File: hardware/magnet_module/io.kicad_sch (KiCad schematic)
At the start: 17 parts, among them J10 Conn_Coaxial, J11 Conn_Coaxial, J12 Conn_Coaxial, J13 Conn_Coaxial, J14 Conn_Coaxial, J15 Conn_Coaxial, J16 Conn_01x04_Pin, J17 Conn_01x04_Pin, J18 Conn_01x03_Pin, J19 Conn_01x03_Pin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

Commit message: add titles & esd protection for IO
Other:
- company: (none) -> Christie Lab, CU-Anschultz
- title: (none) -> Autotrainer Magnet Module - External IO
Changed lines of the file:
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@@
 	(generator_version "8.0")
 	(paper "A4")
+	(title_block
+		(title "Autotrainer Magnet Module - External IO")
+		(date "2024-07-09")
+		(rev "v1.0")
+		(company "Christie Lab, CU-Anschultz")
+		(comment 1 "Prepared by LeafLabs, LLC")
+	)
 	(junction
 		(at 45.72 35.56)

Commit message: add all PNs, relevant datasheets, and test points
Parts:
- C20, C21, C22, C23: footprint (none) -> Capacitor_SMD:C_0603_1608Metric; MPN (none) -> CC0603KRX7R7BB104
- J10, J11, J12, J13, J14, J15: MPN (none) -> CONMHF1-SMD-T
- J16, J17: MPN (none) -> BM04B-SRSS-TB
- J18, J19: MPN (none) -> BM03B-SRSS-TB
- R12, R13: MPN (none) -> RC0603FR-0710KL
- U10: MPN (none) -> TXB0104RUT
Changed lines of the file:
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@@
 			)
 		)
-		(property "Footprint" ""
+		(property "Footprint" "Capacitor_SMD:C_0603_1608Metric"
 			(at 46.0248 71.12 0)
 			(effects
@@
 			)
 		)
-		(property "MPN" ""
+		(property "MPN" "CC0603KRX7R7BB104"
 			(at 46.99 67.31 0)
 			(effects
@@
 			)
 		)
+		(property "MPN" "BM03B-SRSS-TB"
+			(at 260.35 82.55 0)
+			(effects
+				(font
+					(size 1.27 1.27)
+				)
+				(hide yes)
+			)
+		)
 		(pin "2"
 		)
@@
 			)
 		)
+		(property "MPN" "BM04B-SRSS-TB"
+			(at 260.35 50.8 0)
+			(effects
+				(font
+					(size 1.27 1.27)
+				)
+				(hide yes)
+			)
+		)
 		(pin "1"
 		)
@@
 			)
 		)
-		(property "MPN" ""
+		(property "MPN" "RC0603FR-0710KL"
 			(at 41.91 31.75 0)
 			(effects
@@
 			)
 		)
+		(property "MPN" "CONMHF1-SMD-T"
+			(at 54.61 35.56 0)
+			(effects
+				(font
+					(size 1.27 1.27)
+				)
+				(hide yes)
+			)
+		)
 		(pin "1"
 		)
@@
 			)
 		)
+		(property "MPN" "CONMHF1-SMD-T"
+			(at 100.33 120.65 0)
+			(effects
+				(font
+					(size 1.27 1.27)
+				)
+				(hide yes)
+			)
+		)
 		(pin "1"
 		)
@@
 			)
 		)
-		(property "Footprint" ""
+		(property "Footprint" "Capacitor_SMD:C_0603_1608Metric"
 			(at 62.23 108.2548 0)
 			(effects
@@
 			)
 		)
-		(property "MPN" ""
+		(property "MPN" "CC0603KRX7R7BB104"
 			(at 58.42 109.22 0)
 			(effects
@@
 		)
 		(property "Description" "coaxial connector (BNC, SMA, SMB, SMC, Cinch/RCA, LEMO, ...)"
+			(at 100.33 135.89 0)
+			(effects
+				(font
+					(size 1.27 1.27)
+				)
+				(hide yes)
+			)
+		)
+		(property "MPN" "CONMHF1-SMD-T"
 			(at 100.33 135.89 0)
 			(effects
@@
 			)
 		)
-		(property "MPN" ""
+		(property "MPN" "RC0603FR-0710KL"
 			(at 43.18 59.69 0)
 			(effects
@@
 			)
 		)
+		(property "MPN" "CONMHF1-SMD-T"
+			(at 100.33 154.94 0)
+			(effects
+				(font
+					(size 1.27 1.27)
+				)
+				(hide yes)
+			)
+		)
 		(pin "1"
 		)
@@
 		)
 		(property "Description" "4-Bit Bidirectional Voltage-Level Translator, Auto Direction Sensing and ±15-kV ESD Protection, 1.2 - 3.6V APort, 1.65 - 5.5V BPort, Texas_PUQFN-12"
+			(at 52.07 129.54 0)
+			(effects
+				(font
+					(size 1.27 1.27)
+				)
+				(hide yes)
+			)
+		)
+		(property "MPN" "TXB0104RUT"
 			(at 52.07 129.54 0)
 			(effects
@@
 			)
 		)
-		(property "Footprint" ""
+		(property "Footprint" "Capacitor_SMD:C_0603_1608Metric"
 			(at 41.91 108.2548 0)
 			(effects
@@
 			)
 		)
-		(property "MPN" ""
+		(property "MPN" "CC0603KRX7R7BB104"
 			(at 45.72 109.22 0)
 			(effects
@@
 			)
 		)
-		(property "Footprint" ""
+		(property "Footprint" "Capacitor_SMD:C_0603_1608Metric"
 			(at 44.7548 43.18 0)
 			(effects
@@
 			)
 		)
-		(property "MPN" ""
+		(property "MPN" "CC0603KRX7R7BB104"
 			(at 45.72 39.37 0)
 			(effects
@@
 			)
 		)
+		(property "MPN" "BM04B-SRSS-TB"
+			(at 260.35 36.83 0)
+			(effects
+				(font
+					(size 1.27 1.27)
+				)
+				(hide yes)
+			)
+		)
 		(pin "1"
 		)
@@
 			)
 		)
+		(property "MPN" "CONMHF1-SMD-T"
+			(at 55.88 63.5 0)
+			(effects
+				(font
+					(size 1.27 1.27)
+				)
+				(hide yes)
+			)
+		)
 		(pin "1"
 		)
@@
 		)
 		(property "Description" "coaxial connector (BNC, SMA, SMB, SMC, Cinch/RCA, LEMO, ...)"
+			(at 100.33 104.14 0)
+			(effects
+				(font
+					(size 1.27 1.27)
+				)
+				(hide yes)
+			)
+		)
+		(property "MPN" "CONMHF1-SMD-T"
 			(at 100.33 104.14 0)
 			(effects
@@
 			(at 260.35 69.85 0)
 			(effects
+				(font
+					(size 1.27 1.27)
+				)
+				(hide yes)
+			)
+		)
+		(property "MPN" "BM03B-SRSS-TB"
+			(at 260.35 69.85 0)
+			(effects

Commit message: make changes as requested by Ryan
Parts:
- removed C22, C23: 0.1uF, Capacitor_SMD:C_0603_1608Metric, symbol Device:C
- removed J12, J13, J14, J15: Conn_Coaxial, symbol Connector:Conn_Coaxial
- removed U10: TXB0104RUT, Package_DFN_QFN:Texas_R-PUQFN-N12, symbol Logic_LevelTranslator:TXB0104RUT
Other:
- note removed: "External Equipment"
- company: Christie Lab, CU-Anschultz -> Christie Lab, CU-Anschutz

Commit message: make changes requested by dan, run ERC
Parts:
- removed J18, J19: Conn_01x03_Pin, symbol Connector:Conn_01x03_Pin
- added J13, J14: Conn_01x02_Pin, symbol Connector:Conn_01x02_Pin
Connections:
- net GND: now also J13.1 (Pin_1), J14.1 (Pin_1)
- net GPIO0: now also J13.2 (Pin_2)
- net GPIO1: now also J14.2 (Pin_2)
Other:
- note added: "Teensy Connection"

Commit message: update PNs for BNC connectors and motor connectors
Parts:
- J10, J11: MPN CONMHF1-SMD-T -> CONBNC002
- J16, J17: MPN BM04B-SRSS-TB -> SM04B-SRSS-TB
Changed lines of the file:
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@@
 			)
 		)
-		(property "MPN" "BM04B-SRSS-TB"
+		(property "MPN" "SM04B-SRSS-TB"
 			(at 260.35 50.8 0)
 			(effects
@@
 			)
 		)
-		(property "MPN" "CONMHF1-SMD-T"
+		(property "MPN" "CONBNC002"
 			(at 54.61 35.56 0)
 			(effects
@@
 			)
 		)
-		(property "MPN" "BM04B-SRSS-TB"
+		(property "MPN" "SM04B-SRSS-TB"
 			(at 260.35 36.83 0)
 			(effects
@@
 			)
 		)
-		(property "MPN" "CONMHF1-SMD-T"
+		(property "MPN" "CONBNC002"
 			(at 55.88 63.5 0)
 			(effects

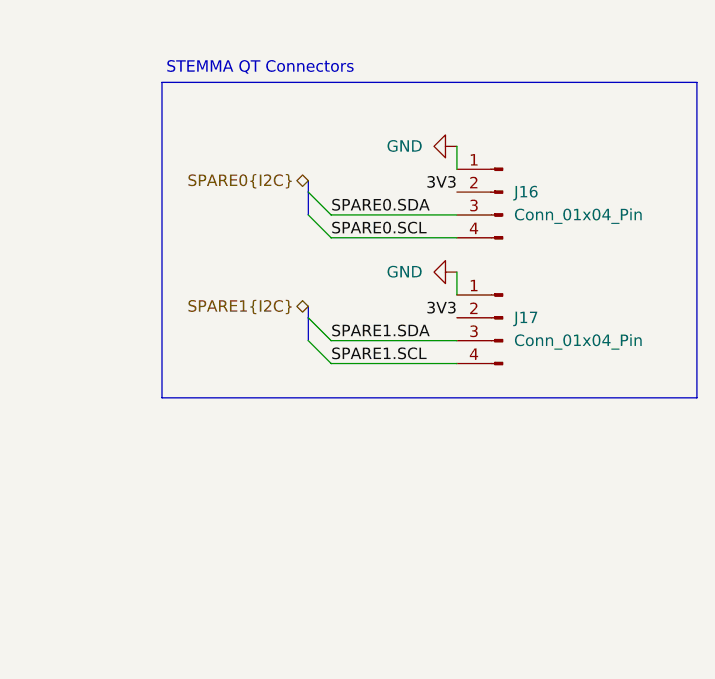
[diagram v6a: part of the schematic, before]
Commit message: add footprints & 3d models for magnet module connector placmeent
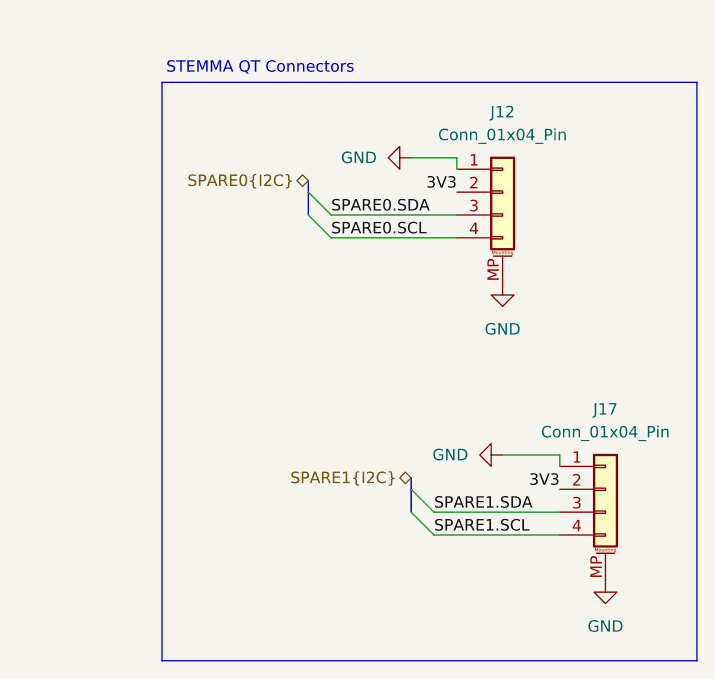
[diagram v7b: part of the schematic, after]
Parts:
- removed J16: Conn_01x04_Pin, symbol Connector:Conn_01x04_Pin
- added J12: Conn_01x04_Pin, Connector_JST:JST_SH_SM04B-SRSS-TB_1x04-1MP_P1.00mm_Horizontal, symbol Connector_Generic_MountingPin:Conn_01x04_MountingPin
- J10, J11: footprint (none) -> Leaf_Connectors:CONBNC002
- J13: footprint (none) -> Connector_PinHeader_2.54mm:PinHeader_1x02_P2.54mm_Horizontal
- J14: footprint (none) -> Connector_PinHeader_2.54mm:PinHeader_1x02_P2.54mm_Horizontal; MPN (none) -> 61300211121
- J17: footprint (none) -> Connector_JST:JST_SH_SM04B-SRSS-TB_1x04-1MP_P1.00mm_Horizontal; symbol Connector:Conn_01x04_Pin -> Connector_Generic_MountingPin:Conn_01x04_MountingPin
- R12, R13: footprint (none) -> Resistor_SMD:R_0603_1608Metric
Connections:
- net 3V3: now also J12.2 (Pin_2)
- net GND: now also J17.MP (MountPin), J12.1 (Pin_1), J12.MP (MountPin)
- net SPARE0.SCL: now also J12.4 (Pin_4)
- net SPARE0.SDA: now also J12.3 (Pin_3)

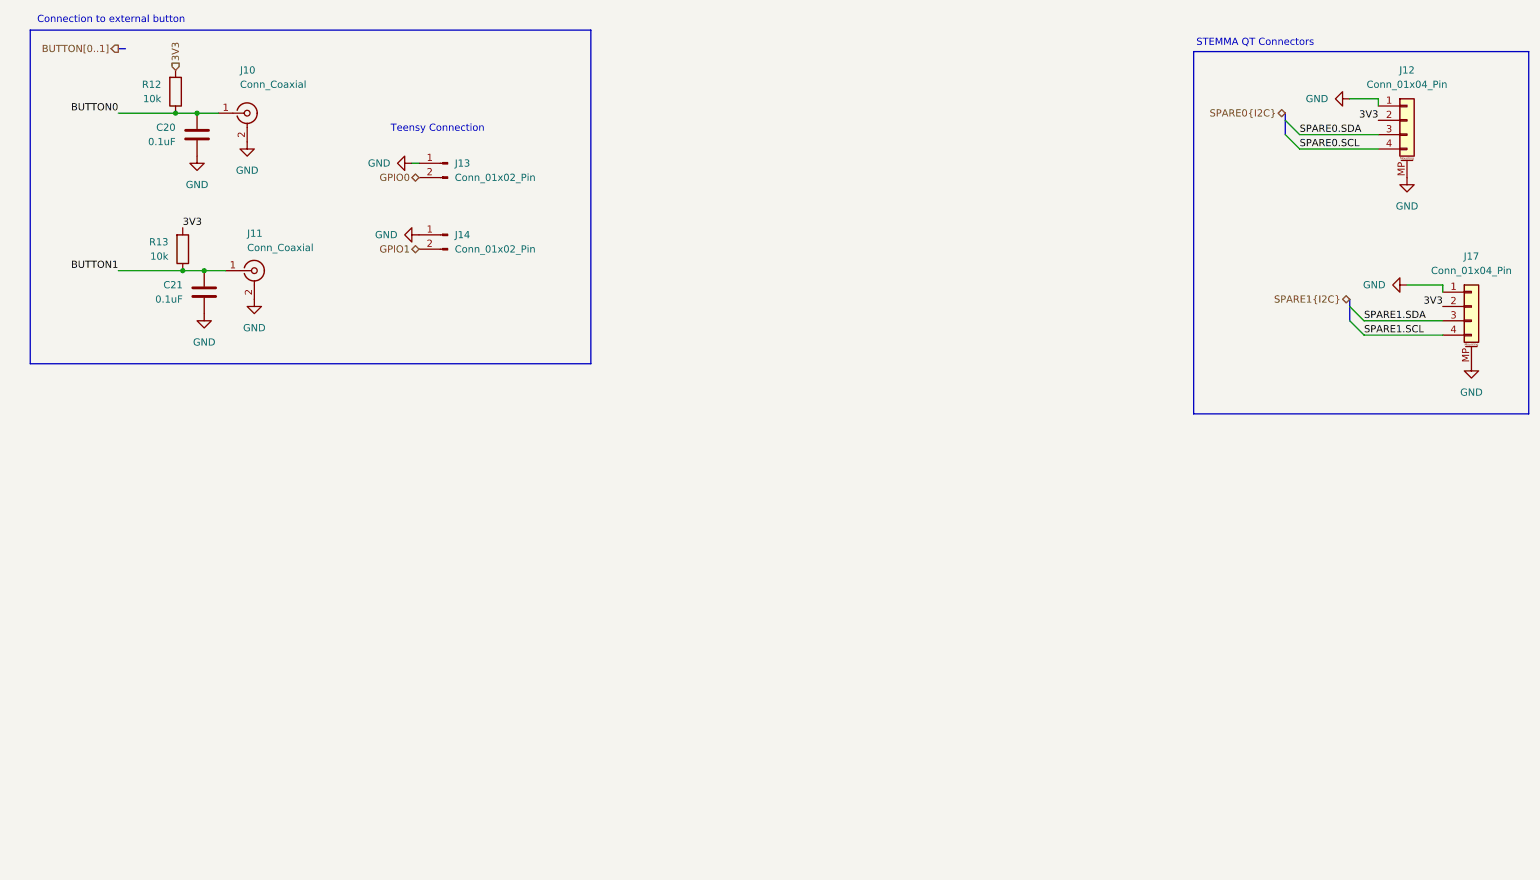
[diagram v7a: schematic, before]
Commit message: Schematic updates to remove button connectors and extra STEMMA QT
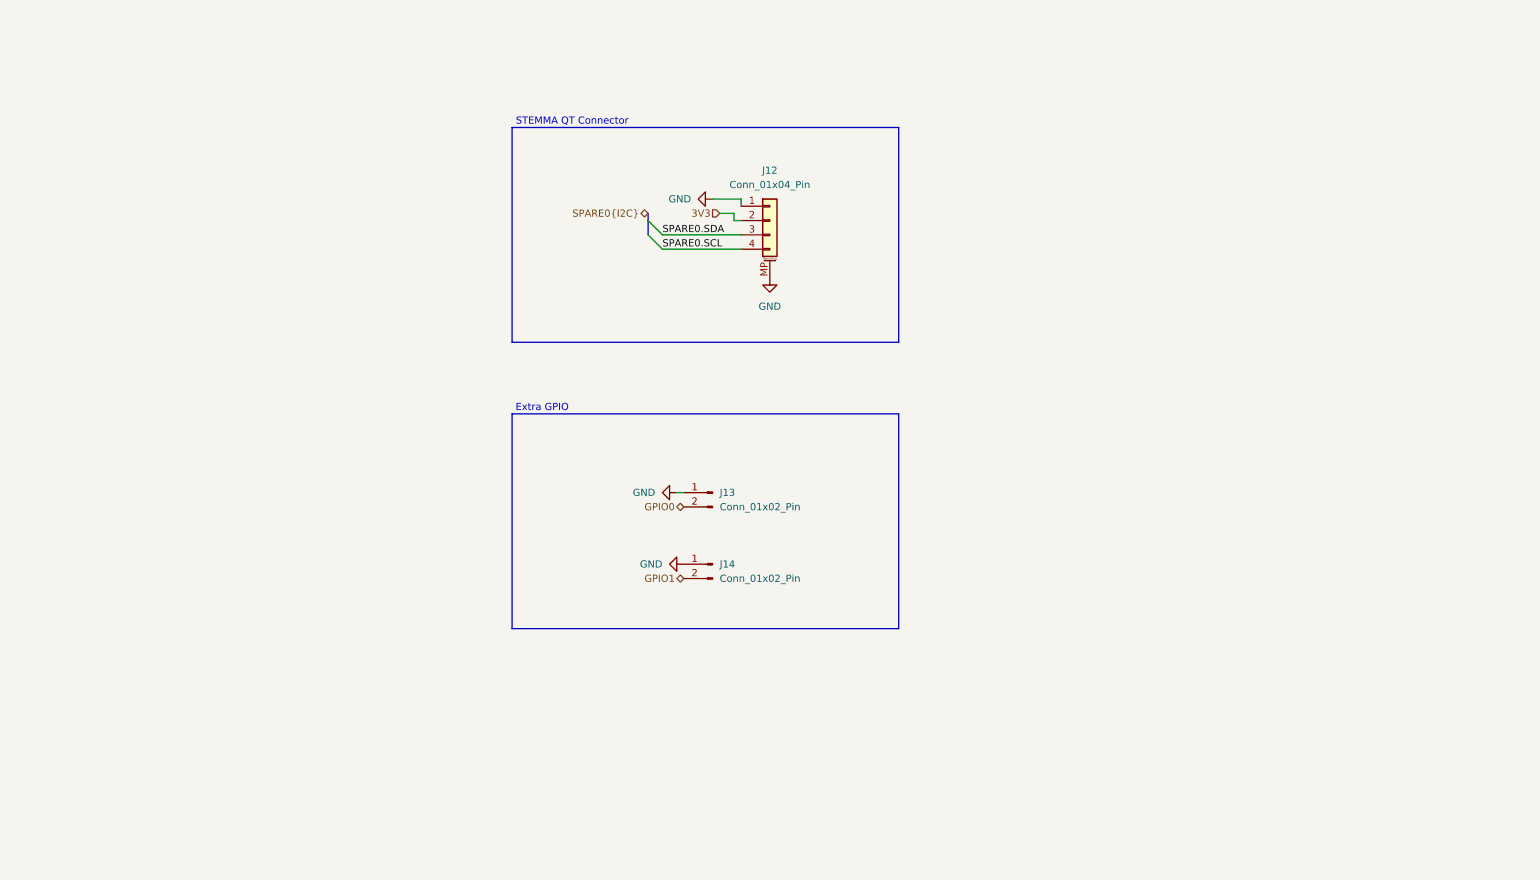
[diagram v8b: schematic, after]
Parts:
- removed C20, C21: 0.1uF, Capacitor_SMD:C_0603_1608Metric, symbol Device:C
- removed J10, J11: Conn_Coaxial, Leaf_Connectors:CONBNC002, symbol Connector:Conn_Coaxial
- removed J17: Conn_01x04_Pin, Connector_JST:JST_SH_SM04B-SRSS-TB_1x04-1MP_P1.00mm_Horizontal, symbol Connector_Generic_MountingPin:Conn_01x04_MountingPin
- removed R12, R13: 10k, Resistor_SMD:R_0603_1608Metric, symbol Device:R
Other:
- note added: "Extra GPIO"
- note added: "STEMMA QT Connector"
- note removed: "Connection to external button"
- note removed: "STEMMA QT Connectors"
- note removed: "Teensy Connection"
- moved on the sheet: J12, J13, J14
